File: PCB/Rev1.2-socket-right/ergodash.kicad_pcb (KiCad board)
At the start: 2 copper layers, 149.9 x 127.4 mm, 83 parts, among them J1 5PIN, SW1 SW_PUSH, SW10 SW_PUSH, SW11 SW_PUSH, SW12 SW_PUSH, SW13 SW_PUSH, SW14 SW_PUSH, SW15 SW_PUSH, SW16 SW_PUSH, SW17 SW_PUSH, SW18 SW_PUSH, SW19 SW_PUSH, SW2 SW_PUSH, SW20 SW_PUSH, SW21 SW_PUSH, SW22 SW_PUSH, SW23 SW_PUSH, SW24 SW_PUSH, SW25 SW_PUSH, SW26 SW_PUSH, SW27 SW_PUSH, SW28 SW_PUSH, SW29 SW_Push, SW3 SW_PUSH, SW30 SW_PUSH, SW31 SW_PUSH, SW32 SW_PUSH, SW33 SW_PUSH, SW34 SW_PUSH, SW35 SW_PUSH, SW4 SW_PUSH, SW40 SW_PUSH, SW5 SW_PUSH, SW6 SW_PUSH, SW7 SW_PUSH, SW8 SW_PUSH, SW9 SW_PUSH, U1 HOLE, U2 HOLE, U3 ProMicro, U4 HOLE, U5 HOLE, U7 HOLE, U8 HOLE, U9 HOLE

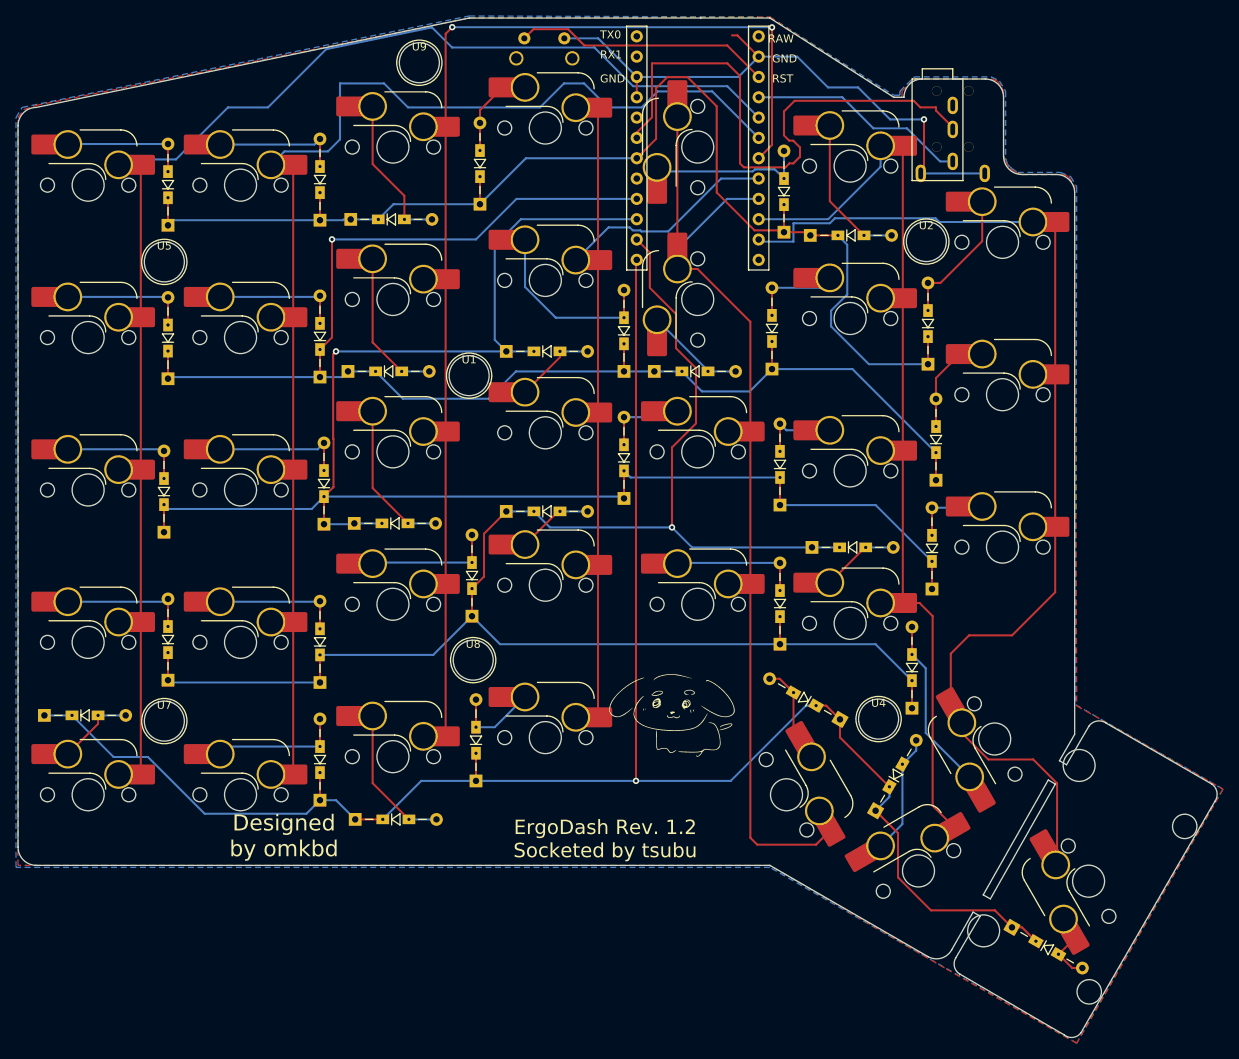
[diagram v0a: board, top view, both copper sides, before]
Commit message: Fix board-edge clearance on right-hand board + regenerate gerbers
Resolve all 11 copper_edge_clearance errors from the previous commit
(0 unrouted, 0 schematic-parity issues confirmed via kicad-cli DRC).
Remaining courtyard violations are by design (U3 Pro Micro under keys,
U1/U2 mounting holes). Regenerated gerbers/drill/zip in ergodash/.

Co-Authored-By: Claude Opus 4.8 <noreply@anthropic.com>
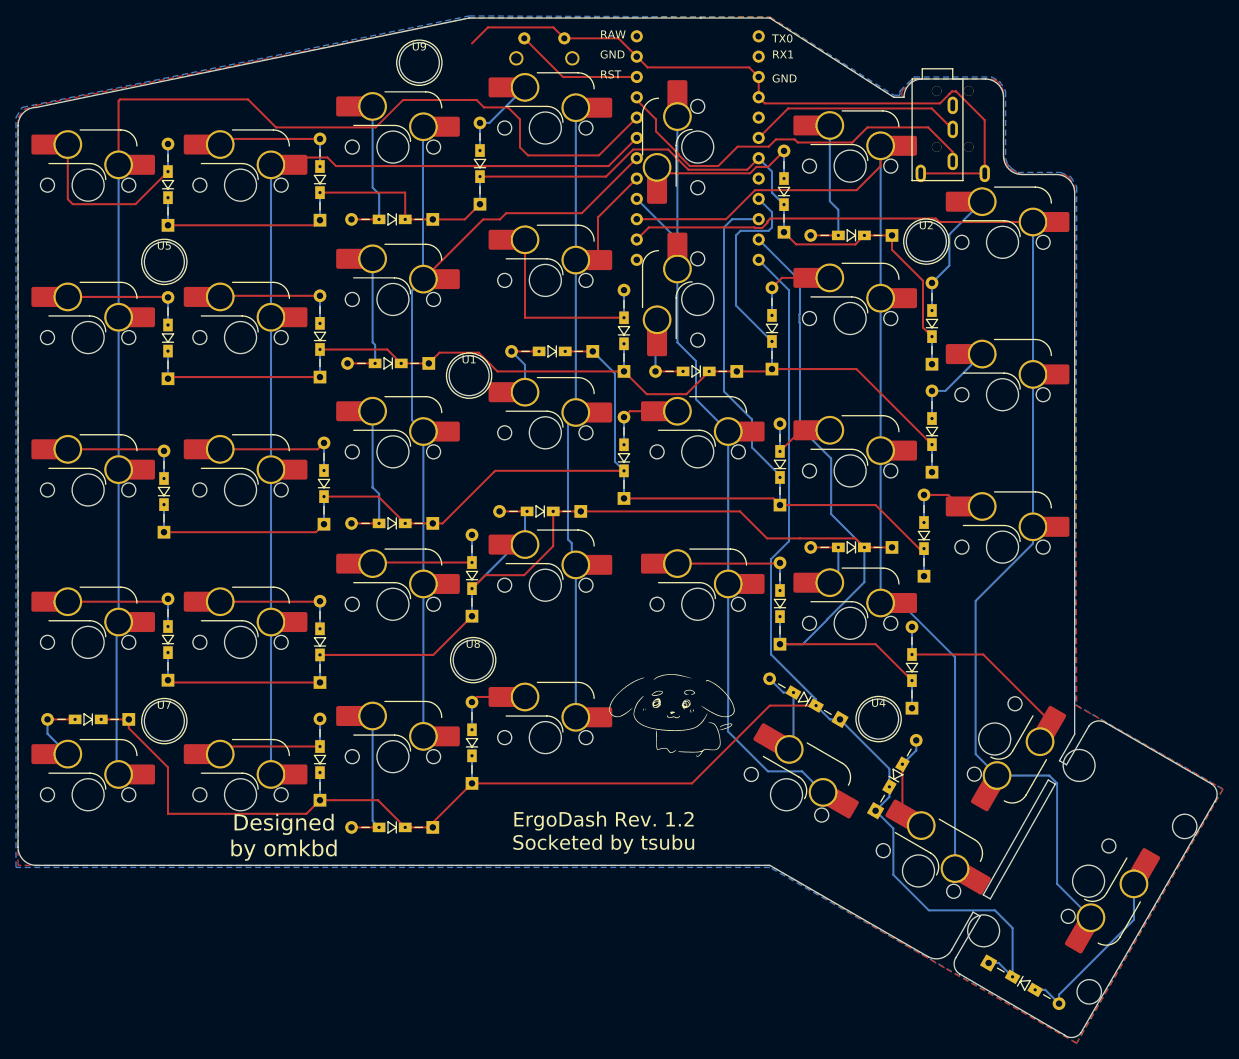
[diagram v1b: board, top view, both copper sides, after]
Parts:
- U3: moved to B.Cu
- moved D15 10.8 mm to (150.1, 78.8), turned to 180 degrees
- moved D29 10.6 mm to (92.1, 124.8), turned to 180 degrees
- moved D18 10.3 mm to (168.1, 81.3), turned to 180 degrees
- moved D9 10.3 mm to (130.1, 62.3), turned to 180 degrees
- moved D21 10.2 mm to (187.5, 64.3), turned to 180 degrees
- moved D10 10.1 mm to (129.6, 80.3), turned to 180 degrees
- moved D24 10.0 mm to (187.5, 103.3), turned to 180 degrees
- moved D11 9.81 mm to (130.1, 100.3), turned to 180 degrees
- moved D31 9.75 mm to (130.1, 138.3), turned to 180 degrees
- moved D16 9.31 mm to (148.6, 98.8), turned to 180 degrees
- moved D68 5.32 mm to (199.6, 155.2)
- moved D27 1.89 mm to (191.5, 106.9)
- moved D26 1.12 mm to (192.5, 93.9)
- moved D32 0.59 mm to (135.0, 132.8)
- moved D25 0.50 mm to (192.5, 80.4)
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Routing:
- net /sda/uart: track 71.2 -> 26.9 mm
- net /col2: track 147.0 -> 110.4 mm, vias 2 -> 0
- net /row1: track 177.5 -> 145.8 mm, vias 1 -> 0
- net /col1: track 152.4 -> 124.2 mm
- net /row2: track 201.3 -> 178.8 mm, vias 1 -> 0
- net /col5: track 109.6 -> 131.5 mm
- net VCC: track 27.6 -> 49.0 mm
- net /col6: track 132.0 -> 150.7 mm
- net /row0: track 153.6 -> 135.0 mm
- net /rst: track 32.2 -> 16.1 mm
- net Net-(D68-A): track 6.55 -> 22.5 mm
- net /col3: track 103.7 -> 89.2 mm
- net GND: track 73.3 -> 87.1 mm, vias 1 -> 0
- net /col4: track 119.0 -> 105.4 mm
- net Net-(D1-A): track 16.0 -> 24.8 mm
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
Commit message: Move U3 outline silkscreen to front + regenerate gerbers (socket-right)
Pro Micro (U3) footprint stays on B.Cu (needed so the USB port clears the
board edge), but its outline markers were still on B.SilkS/B.Fab, making
the mounting-side indicator show on the wrong physical face. Moved just
the outline graphics (courtyard rectangle) to F.SilkS/F.Fab without
touching pads or footprint placement. DRC confirms 0 unrouted, no new
violations (silk_overlap actually dropped 38->33). Regenerated gerbers,
drills and the upload zip in ergodash/.

Co-Authored-By: Claude <noreply@anthropic.com>
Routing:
- net /row3: track 204.9 -> 198.8 mm
- net Net-(D25-A): track 16.2 -> 19.8 mm
- net /col0: track 159.6 -> 158.8 mm
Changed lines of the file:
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@@
 		(property "Reference" "U3"
 			(at 0 -2 90)
-			(layer "B.SilkS")
+			(layer "F.SilkS")
 			(hide yes)
 			(effects
@@
 					(thickness 0.15)
 				)
-				(justify mirror)
 			)
 		)
@@
 		(duplicate_pad_numbers_are_jumpers no)
 		(fp_line
-			(start 8.89 15.24)
-			(end 8.89 -15.24)
+			(start 9 15.24)
+			(end 9 -15.5)
 			(stroke
-				(width 0.15)
-				(type solid)
+				(width 0.1)
+				(type default)
 			)
-			(layer "B.SilkS")
+			(layer "F.SilkS")
 		)
 		(fp_line
-			(start 8.89 -15.24)
-			(end 6.35 -15.24)
+			(start 9 -15.5)
+			(end 6 -15.5)
 			(stroke
-				(width 0.15)
-				(type solid)
+				(width 0.1)
+				(type default)
 			)
-			(layer "B.SilkS")
+			(layer "F.SilkS")
 		)
 		(fp_line
-			(start 6.35 15.24)
-			(end 8.89 15.24)
+			(start 6 15.24)
+			(end 9 15.24)
 			(stroke
-				(width 0.15)
-				(type solid)
+				(width 0.1)
+				(type default)
 			)
-			(layer "B.SilkS")
+			(layer "F.SilkS")
 		)
 		(fp_line
-			(start 6.35 -15.24)
-			(end 6.35 15.24)
+			(start 6 -15.5)
+			(end 6 15.24)
 			(stroke
-				(width 0.15)
-				(type solid)
+				(width 0.1)
+				(type default)
 			)
-			(layer "B.SilkS")
+			(layer "F.SilkS")
 		)
 		(fp_line
-			(start -6.35 15.24)
-			(end -6.35 -15.24)
+			(start -6 15.5)
+			(end -6 -15.5)
 			(stroke
-				(width 0.15)
-				(type solid)
+				(width 0.1)
+				(type default)
 			)
-			(layer "B.SilkS")
+			(layer "F.SilkS")
 		)
 		(fp_line
-			(start -6.35 -15.24)
-			(end -8.89 -15.24)
+			(start -6 -15.5)
+			(end -9 -15.5)
 			(stroke
-				(width 0.15)
-				(type solid)
+				(width 0.1)
+				(type default)
 			)
-			(layer "B.SilkS")
+			(layer "F.SilkS")
 		)
 		(fp_line
-			(start -8.89 15.24)
-			(end -6.35 15.24)
+			(start -9 15.5)
+			(end -6 15.5)
 			(stroke
-				(width 0.15)
-				(type solid)
+				(width 0.1)
+				(type default)
 			)
-			(layer "B.SilkS")
+			(layer "F.SilkS")
 		)
 		(fp_line
-			(start -8.89 -15.24)
-			(end -8.89 15.24)
+			(start -9 -15.5)
+			(end -9 15.5)
 			(stroke
-				(width 0.15)
-				(type solid)
+				(width 0.1)
+				(type default)
 			)
-			(layer "B.SilkS")
+			(layer "F.SilkS")
 		)
 		(fp_line
@@
 	(segment
 		(start 134.978 108.406)
-		(end 139.268 104.116)
-		(width 0.254)
-		(layer "B.Cu")
-		(net "/row3")
-	)
-	(segment
-		(start 134.978 108.406)
 		(end 134.978 111.856)
 		(width 0.254)
@@
 	)
 	(segment
-		(start 122.555 95.756)
-		(end 122.555 86.233)
+		(start 122.555 95.833)
+		(end 123.291 96.569)
 		(width 0.254)
 		(layer "B.Cu")
@@
 	)
 	(segment
-		(start 123.368 96.569)
-		(end 122.555 95.756)
+		(start 122.555 86.233)
+		(end 122.555 95.833)
 		(width 0.254)
 		(layer "B.Cu")
@@
 	)
 	(segment
-		(start 122.555 95.833)
-		(end 122.555 95.756)
+		(start 123.368 96.569)
+		(end 123.368 100.256)
 		(width 0.254)
 		(layer "B.Cu")
@@
 	)
 	(segment
-		(start 123.368 100.256)
+		(start 123.291 96.569)
 		(end 123.368 96.569)
 		(width 0.254)
@@
 	)
 	(segment
-		(start 194.647 64.14725)
-		(end 194.647 68.027)
+		(start 192.478 73.646)
+		(end 192.478 70.196)
 		(width 0.254)
 		(layer "B.Cu")
@@
 	)
 	(segment
-		(start 192.478 73.646)
-		(end 192.478 70.196)
+		(start 198.478 70.256)
+		(end 192.538 70.256)
+		(width 0.254)
+		(layer "B.Cu")
+		(net "Net-(D25-A)")
+	)
+	(segment
+		(start 198.755 69.979)
+		(end 198.478 70.256)
 		(width 0.254)
 		(layer "B.Cu")
@@
 	(segment
 		(start 198.755 60.03925)
-		(end 194.647 64.14725)
+		(end 198.755 69.979)
 		(width 0.254)
 		(layer "B.Cu")
@@
 	)
 	(segment
-		(start 194.647 68.027)
+		(start 192.538 70.256)
 		(end 192.478 70.196)
 		(width 0.254)
@@
 	)
 	(segment
-		(start 172.27208 62.147)
-		(end 171.904 62.51508)
+		(start 171.904 62.681079)
+		(end 171.266079 63.319)
 		(width 0.254)
 		(layer "F.Cu")
@@
 	)
 	(segment
-		(start 205.105 62.57925)
-		(end 193.393942 62.57925)
+		(start 172.66308 61.756)
+		(end 171.904 62.51508)
 		(width 0.254)
 		(layer "F.Cu")
@@
 	)
 	(segment
-		(start 171.266079 63.319)
-		(end 170.363921 63.319)
+		(start 171.904 62.51508)
+		(end 171.904 62.681079)
 		(width 0.254)
 		(layer "F.Cu")
@@
 	)
 	(segment
-		(start 192.961692 62.147)
-		(end 172.27208 62.147)
+		(start 193.978 61.756)
+		(end 172.66308 61.756)
 		(width 0.254)
 		(layer "F.Cu")
@@
 	)
 	(segment
-		(start 171.904 62.681079)
-		(end 171.266079 63.319)
+		(start 170.300921 63.256)
+		(end 157.089 63.256)
 		(width 0.254)
 		(layer "F.Cu")
@@
 	)
 	(segment
-		(start 170.300921 63.256)
-		(end 157.089 63.256)
+		(start 170.363921 63.319)
+		(end 170.300921 63.256)
 		(width 0.254)
 		(layer "F.Cu")
@@
 	)
 	(segment
-		(start 171.904 62.51508)
-		(end 171.904 62.681079)
+		(start 157.089 63.256)
+		(end 155.575 64.77)
 		(width 0.254)
 		(layer "F.Cu")
@@
 	)
 	(segment
-		(start 193.393942 62.57925)
-		(end 192.961692 62.147)
+		(start 205.105 62.57925)
+		(end 194.80125 62.57925)
 		(width 0.254)
 		(layer "F.Cu")
@@
 	)
 	(segment
-		(start 157.089 63.256)
-		(end 155.575 64.77)
+		(start 171.266079 63.319)
+		(end 170.363921 63.319)
 		(width 0.254)
 		(layer "F.Cu")
@@
 	)
 	(segment
-		(start 170.363921 63.319)
-		(end 170.300921 63.256)
+		(start 194.80125 62.57925)
+		(end 193.978 61.756)
 		(width 0.254)
 		(layer "F.Cu")
@@
 	)
 	(segment
-		(start 90.805 55.4355)
-		(end 90.805 47.429)
+		(start 93.58 55.4355)
+		(end 93.993 55.0225)
 		(width 0.254)
 		(layer "F.Cu")
@@
 	)
 	(segment
-		(start 93.58 55.4355)
-		(end 93.993 55.0225)
+		(start 140.978 49.756)
+		(end 139.478 48.256)
 		(width 0.254)
 		(layer "F.Cu")
@@
 	)
 	(segment
-		(start 90.805 47.429)
-		(end 90.978 47.256)
+		(start 135.55075 47.32875)
+		(end 126.367283 47.32875)
 		(width 0.254)
 		(layer "F.Cu")
@@
 	)
 	(segment
-		(start 141.978 54.256)
-		(end 140.978 53.256)
+		(start 90.978 47.256)
+		(end 90.805 47.429)
 		(width 0.254)
 		(layer "F.Cu")
@@
 	)
 	(segment
-		(start 155.575 49.53)
-		(end 150.849 54.256)
+		(start 109.478 44.756)
+		(end 106.978 47.256)
 		(width 0.254)
 		(layer "F.Cu")
@@
 	)
 	(segment
-		(start 136.478 48.256)
-		(end 135.55075 47.32875)
+		(start 140.978 53.256)
+		(end 140.978 49.756)
 		(width 0.254)
 		(layer "F.Cu")
@@
 	)
 	(segment
-		(start 135.55075 47.32875)
-		(end 126.367283 47.32875)
+		(start 136.478 48.256)
+		(end 135.55075 47.32875)
 		(width 0.254)
 		(layer "F.Cu")
@@
 	)
 	(segment
-		(start 122.940033 50.756)
-		(end 110.478 50.756)
+		(start 141.978 54.256)
+		(end 140.978 53.256)
 		(width 0.254)
 		(layer "F.Cu")
@@
 	)
 	(segment
-		(start 139.478 48.256)
-		(end 136.478 48.256)
+		(start 106.978 47.256)
+		(end 90.978 47.256)
 		(width 0.254)
 		(layer "F.Cu")
@@
 	)
 	(segment
-		(start 140.978 53.256)
-		(end 140.978 49.756)
+		(start 126.367283 47.32875)
+		(end 123.794533 44.756)
 		(width 0.254)
 		(layer "F.Cu")
@@
 	)
 	(segment
-		(start 90.978 47.256)
-		(end 106.978 47.256)
+		(start 155.575 49.53)
+		(end 150.849 54.256)
 		(width 0.254)
 		(layer "F.Cu")
@@
 	)
 	(segment
-		(start 126.367283 47.32875)
-		(end 122.940033 50.756)
+		(start 123.794533 44.756)
+		(end 109.478 44.756)
 		(width 0.254)
 		(layer "F.Cu")
@@
 	)
 	(segment
-		(start 150.849 54.256)
-		(end 141.978 54.256)
+		(start 139.478 48.256)
+		(end 136.478 48.256)
 		(width 0.254)
 		(layer "F.Cu")
@@
 	)
 	(segment
-		(start 110.478 50.756)
-		(end 106.978 47.256)
+		(start 90.805 47.429)
+		(end 90.805 55.4355)
 		(width 0.254)
 		(layer "F.Cu")
@@
 	)
 	(segment
-		(start 140.978 49.756)
-		(end 139.478 48.256)
+		(start 150.849 54.256)
+		(end 141.978 54.256)
 		(width 0.254)
 		(layer "F.Cu")
